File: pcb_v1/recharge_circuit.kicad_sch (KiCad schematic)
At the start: 23 parts, among them J2 power Switch, J5 10x1mm FFC/FPC, M1 DMG6968U-7_single, M2 DMG6968U-7_single, Q1 DMG6968UMD, U4 MCP1825S, U5 AP9101CK, U6 MCP73831-2-OT

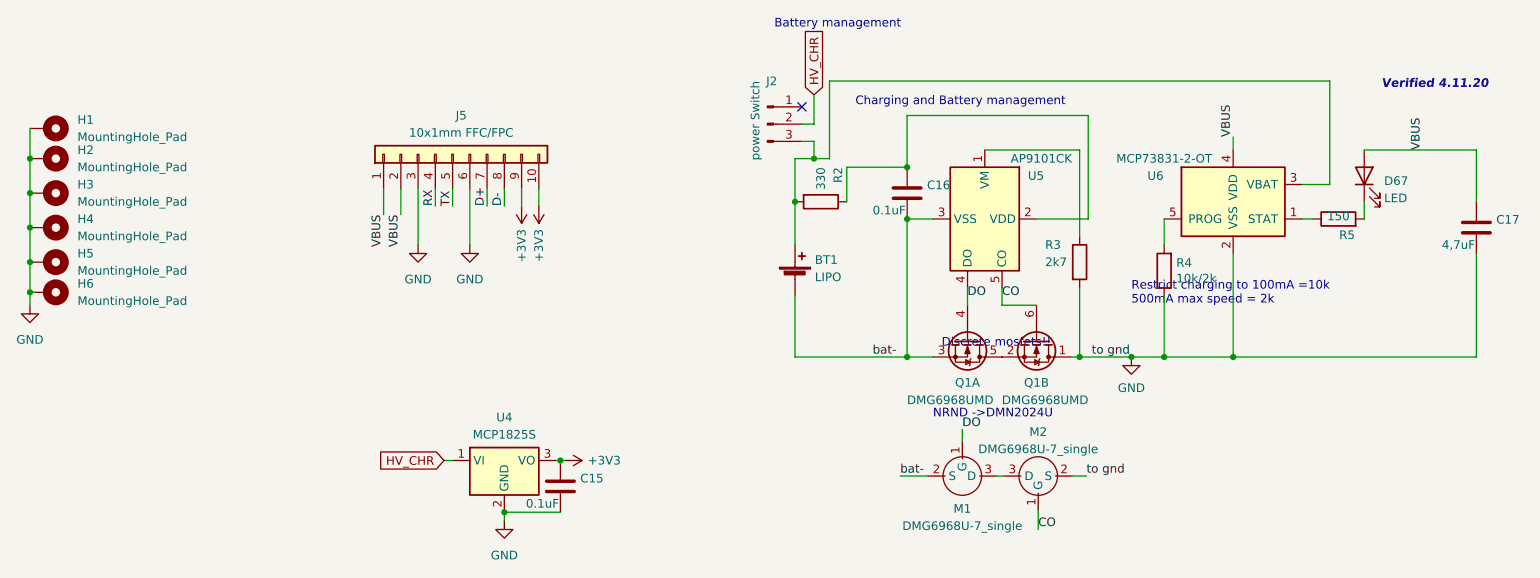
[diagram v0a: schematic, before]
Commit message: Re-drew PCB. Flipped to the correct orientation
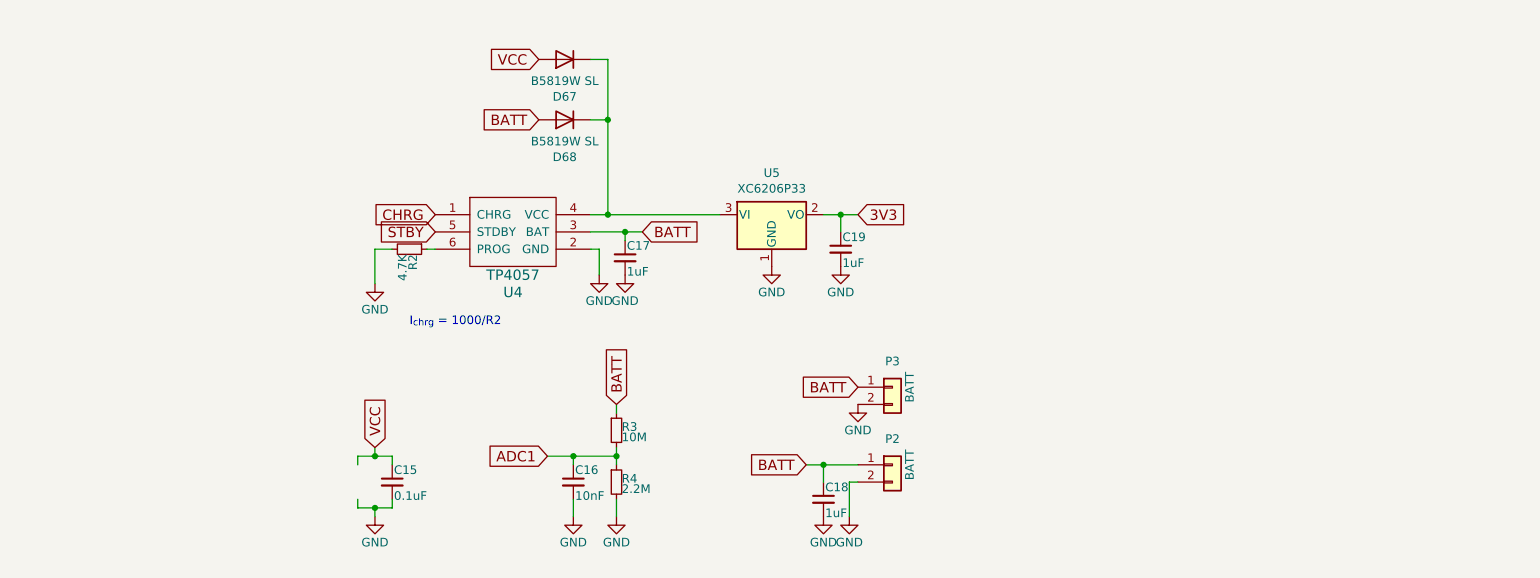
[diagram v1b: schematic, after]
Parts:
- removed BT1: LIPO, Connector_PinHeader_2.54mm:PinHeader_1x02_P2.54mm_Vertical_SMD_Pin1Left, symbol Device:Battery_Cell
- removed C15, C16: 0.1uF, Capacitor_SMD:C_0603_1608Metric, symbol FL01_smol-rescue:C-Device
- removed C17: 4,7uF, Capacitor_SMD:C_0603_1608Metric, symbol FL01_smol-rescue:C-Device
- removed D67: LED, LED_SMD:LED_0603_1608Metric, symbol Device:LED
- removed H1, H2, H3, H4, H5, H6: MountingHole_Pad, MountingHole:MountingHole_3.2mm_M3_DIN965_Pad, symbol Mechanical:MountingHole_Pad
- removed J2: power Switch, Connector_PinHeader_2.54mm:PinHeader_1x03_P2.54mm_Vertical_SMD_Pin1Left, symbol Connector:Conn_01x03_Male
- removed J5: 10x1mm FFC/FPC, Connector_FFC-FPC:Molex_200528-0100_1x10-1MP_P1.00mm_Horizontal, symbol Connector_Generic:Conn_01x10
- removed M1, M2: DMG6968U-7_single, Package_TO_SOT_SMD:TSOT-23, symbol dmg6968u-7CUSTOM:DMG6968U-7_single
- removed Q1: DMG6968UMD, Package_TO_SOT_SMD:SOT-23-6_Handsoldering, symbol FL01_smol-rescue:DMG6968UMD-DMG6968UMD
- removed R2: 330, Resistor_SMD:R_0603_1608Metric, symbol FL01_smol-rescue:R-Device
- removed R3: 2k7, Resistor_SMD:R_0603_1608Metric, symbol FL01_smol-rescue:R-Device
- removed R4: 10k/2k, Resistor_SMD:R_0603_1608Metric, symbol FL01_smol-rescue:R-Device
- removed R5: 150, Resistor_SMD:R_0603_1608Metric, symbol FL01_smol-rescue:R-Device
- removed U4: MCP1825S, Package_TO_SOT_SMD:SOT-223-3_TabPin2, symbol Regulator_Linear:MCP1825S
- removed U5: AP9101CK, Package_TO_SOT_SMD:SOT-23-5, symbol FL01_smol-rescue:AP9101CK-Battery_Management
- removed U6: MCP73831-2-OT, Package_TO_SOT_SMD:SOT-23-5, symbol FL01_smol-rescue:MCP73831-2-OT-Battery_Management
- added C15: 0.1uF, Capacitor_SMD:C_0805_2012Metric, symbol Device:C_Small
- added C16: 10nF, Capacitor_SMD:C_0805_2012Metric, symbol Device:C_Small
- added C17, C18, C19: 1uF, Capacitor_SMD:C_0805_2012Metric, symbol Device:C_Small
- added D67, D68: B5819W SL, Diode_SMD:D_SOD-123, symbol Device:D
- added P2: BATT, Connector_PinHeader_2.54mm:PinHeader_1x02_P2.54mm_Vertical, symbol Connector_Generic:Conn_01x02
- added P3: BATT, Connector_PinSocket_2.00mm:PinSocket_1x02_P2.00mm_Vertical, symbol Connector_Generic:Conn_01x02
- added R2: 4.7K, Resistor_SMD:R_0805_2012Metric, symbol Device:R_Small
- added R3: 10M, Resistor_SMD:R_0805_2012Metric, symbol Device:R_Small
- added R4: 2.2M, Resistor_SMD:R_0805_2012Metric, symbol Device:R_Small
- added U4: TP4057, Package_TO_SOT_SMD:SOT-23-6, symbol custom:TP4057
- added U5: XC6206P33, Package_TO_SOT_SMD:SOT-23, symbol Regulator_Linear:AP2127N-3.0
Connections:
- net GND: now also C15.2, C16.2, C17.2, C18.2, C19.2, P2.2 (Pin_2), P3.2 (Pin_2), R2.2, R4.2, U4.2 (GND), U5.1 (GND)
- new net: R2.1, U4.6 (PROG)
- new net: D67.1 (K), D68.1 (K), U4.4 (VCC), U5.3 (VI)
- new net 3V3: C19.1, U5.2 (VO)
- new net ADC1: C16.1, R3.2, R4.1
- new net BATT: C17.1, C18.1, D68.2 (A), P2.1 (Pin_1), P3.1 (Pin_1), R3.1, U4.3 (BAT)
- new net CHRG: U4.1 (CHRG)
- new net STBY: U4.5 (STDBY)
- new net VCC: C15.1, D67.2 (A)
- no-connect marks 1 -> 0
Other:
- note added: "I_{chrg} = 1000/R2"
- note removed: "Battery management"
- note removed: "Charging and Battery management"
- note removed: "Discrete mosfets!!"
- note removed: "NRND ->DMN2024U"
- note removed: "Restrict charging to 100mA =10k 500mA max speed = 2k"
- note removed: "Verified 4.11.20"
